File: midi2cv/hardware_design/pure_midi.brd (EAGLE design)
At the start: 78.9 x 100 mm, 117 parts, among them IC1 STM32F373C, IC2 AD5754BREZ, IC3 TL074D, IC4 TL072D, IC5 6N138SMD, IC6 LD117AS33TR, IC7 LD117AS50TR, IC8 ADR435, IC9 ADR431, J1 CORTEX_DEBUG_PTH, SW1 EC12E_SW, U2 AD5676ARUZ, U4 MAX3421, X1 ABRACON_ABM3B-8.000MHZ-B2-TAB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, X10 WQP-PJ301M-12_JACK, X11 WQP-PJ301M-12_JACK, X12 WQP-PJ301M-12_JACK, X13 WQP-PJ301M-12_JACK, X14 WQP-PJ301M-12_JACK, X15 WQP-PJ301M-12_JACK, X16 WQP-PJ301M-12_JACK, X17 WQP-PJ301M-12_JACK, X18 WQP-PJ301M-12_JACK, X19 WQP-PJ301M-12_JACK, X2 KUSBVX-BS1N, X20 WQP-PJ301M-12_JACK, X21 OG-MIDI_MAB5SHCUI-SD-50BV, X22 OG-MIDI_MAB5SHCUI-SD-50BV, X23 KUSBVX, X24 ABRACON_ABM3B-12.000MHZ-B2-TA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, X3 WQP-PJ301M-12_JACK, X4 WQP-PJ301M-12_JACK, X5 WQP-PJ301M-12_JACK, X6 WQP-PJ301M-12_JACK, X7 WQP-PJ301M-12_JACK, X8 WQP-PJ301M-12_JACK, X9 WQP-PJ301M-12_JACK

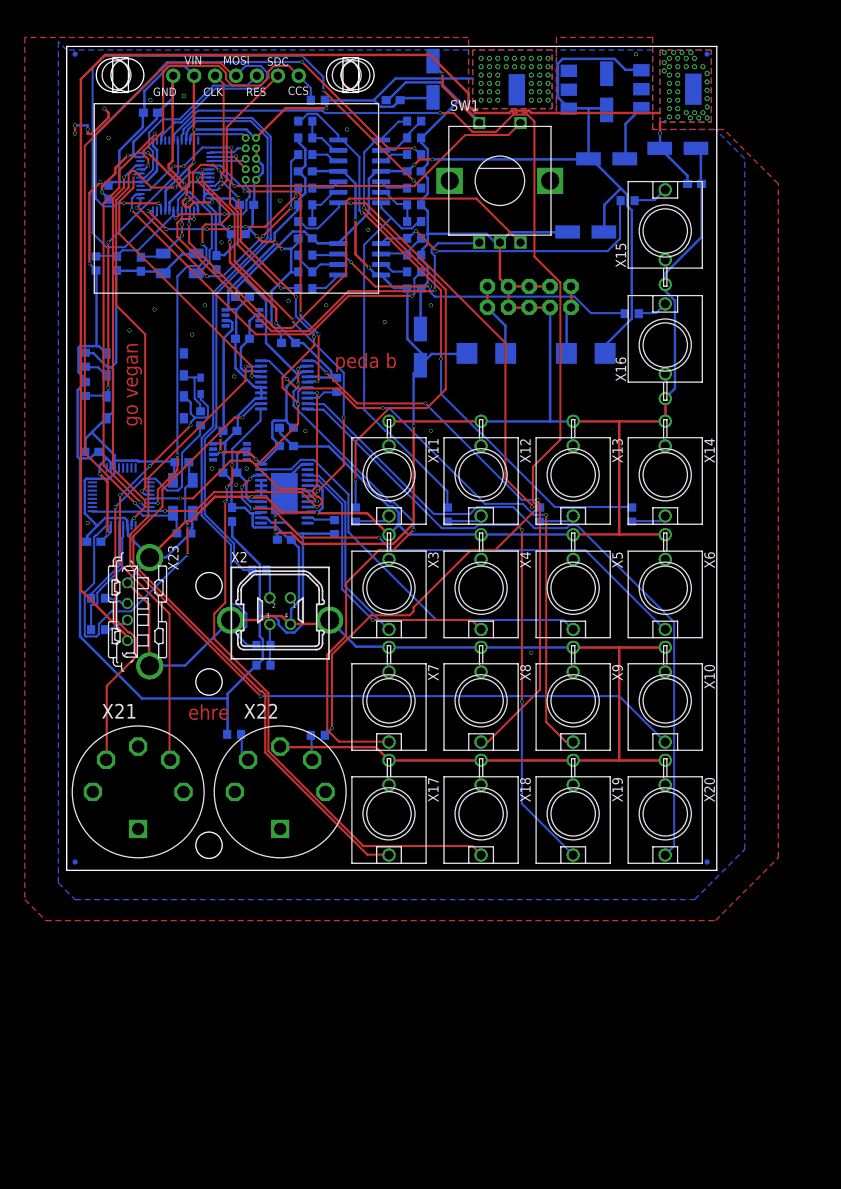
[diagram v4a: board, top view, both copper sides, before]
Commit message: Remove usb from midi
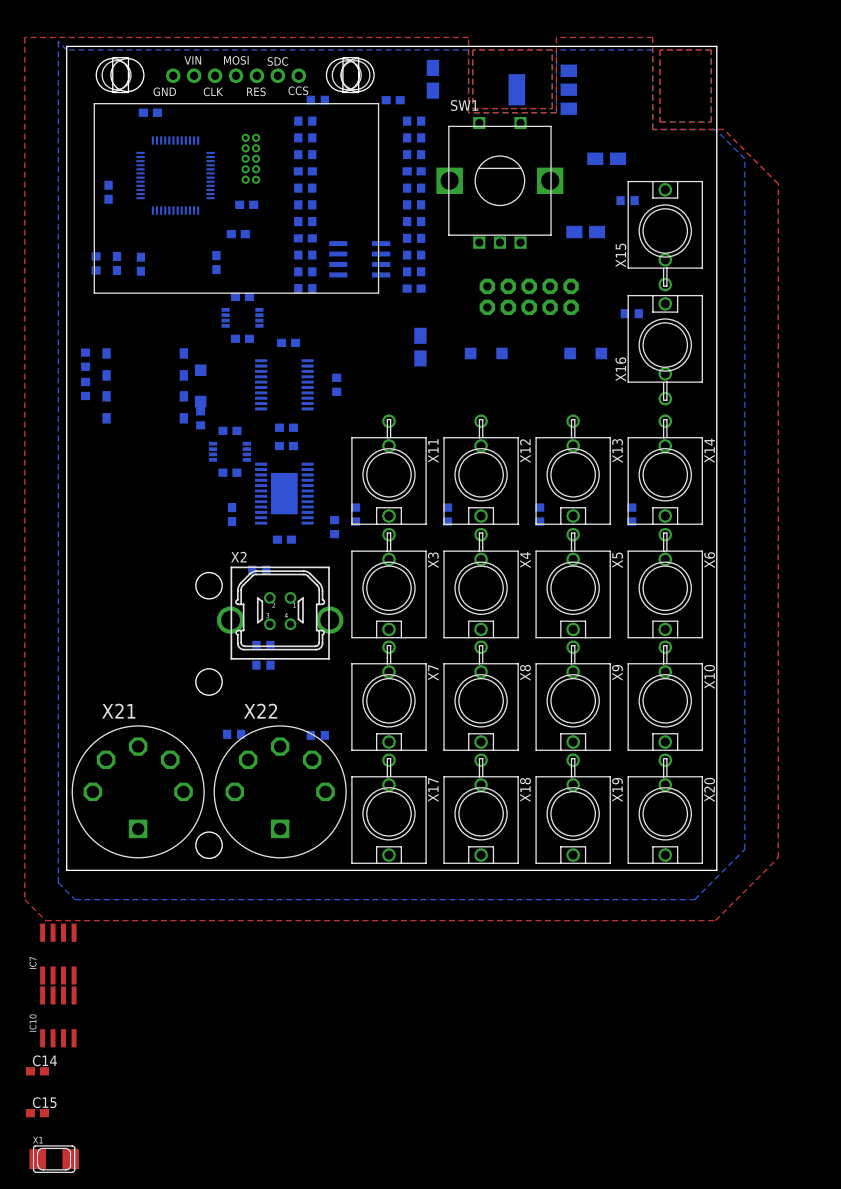
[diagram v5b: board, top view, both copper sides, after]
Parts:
- removed C16, C17: 100n, rcl:C0603
- removed C21, C23: 22u, GMSN:153CLV-0505
- removed C24: 100nF, rcl:C0603
- removed FD1, FD2, FD3, FD4: FIDUCIALUFIDUCIAL, SparkFun-Aesthetics:FIDUCIAL-MICRO
- removed IC3: TL074D, linear:SO14
- removed R21, R22: 22R, rcl:R0603
- removed U4: MAX3421, SparkFun-IC-Comms:TQFP32-5MM
- removed X23: KUSBVX, con-kycon:KUSBVX
- removed X24: ABRACON_ABM3B-12.000MHZ-B2-TABRACON_ABM3B-12.000MHZ-B2-T_0_0, Abracon - ABM3B-12.000MHZ-B2-T:ABRACON_ABM3B-12.000MHZ-B2-T_0
- added IC10: TL072CD, jhbruhn-opamp:SOIC8
- C1, C10, C11, C12, C13, C2, C25, C26, C27, C28, C29, C3, C30, C31, C32, C4, C5, C6, C7, C8, C9: device rcl:C0603 -> jhbruhn-cdr:C0603
- C14, C15: value 22p -> 100n; device rcl:C0603 -> jhbruhn-cdr:C0603
- C18, C19, C20, C22: value 22u -> 10uF; device GMSN:153CLV-0505 -> jhbruhn-cdr:CASE-A_3216
- D2: value 1N4148 -> 1N4148W; device adafruit:SOD-323F -> jhbruhn-cdr:SOD123
- D3, D4: value 1N4001 -> B5819W; device GMSN:SMADIODE -> jhbruhn-cdr:SOD123
- IC4: value TL072D -> TL072CD; device linear:SO08 -> jhbruhn-opamp:SOIC8
- IC7: value LD117AS50TR -> TL072CD; device v-reg:SOT223 -> jhbruhn-opamp:SOIC8
- R1, R10, R11, R12, R13, R14, R15, R16, R17, R18, R19, R2, R20, R23, R24, R25, R26, R27, R28, R29, R3, R30, R31, R32, R33, R34, R35, R36, R37, R38, R39, R4, R40, R6, R7: device rcl:R0603 -> jhbruhn-cdr:R0603
- R5: device resistor:R0603 -> jhbruhn-cdr:R0603
- X1: value ABRACON_ABM3B-8.000MHZ-B2-TABRACON_ABM3B-8.000MHZ-B2-T_0_0 -> 8MHz; device Abracon - ABM3B-8.000MHZ-B2-T:ABRACON_ABM3B-8.000MHZ-B2-T_0 -> jhbruhn-cdr:NX5032
- moved IC7 128.4 mm to (-1.02, -10.2), flipped to the top, turned to 0 degrees
- moved X1 109.8 mm to (-1.52, -35.1), flipped to the top, turned to 0 degrees
- moved C15 80.9 mm to (-3.56, -29.5), flipped to the top, turned to 0 degrees
- moved C14 67.7 mm to (-3.56, -24.4), flipped to the top
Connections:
- removed net +5V: C21.+, C24.1, IC7.4, X23.1
- removed net N$7: C14.2, U4.25, X24.1
- removed net USB_D_N: R22.1, X23.2
- removed net USB_D_P: R21.1, X23.3
- removed net USB_N: R22.2, U4.20
- removed net USB_P: R21.2, U4.21
- net +12V: now also C14.1, IC10.8, IC7.8; no longer C23.+, IC3.4, IC7.3
- net +3V3: no longer C16.1, C17.1, U4.2, U4.23
- net -12V: now also C15.2, IC10.4, IC7.4; no longer IC3.11
- net GND: now also C14.2; no longer C14.1, C16.2, C17.2, C18.-, C19.+, C21.-, C23.-, C24.2, IC7.1, PWR1.3, PWR1.4, PWR1.5, PWR1.6, PWR1.7, PWR1.8, U4.19, U4.3, X1.2, X1.4, X23.4, X23.M1, X23.M2, X24.2, X24.4
- net INT_USB: no longer U4.18
- net MISO: no longer U4.15
- net MOSI: no longer U4.16
- net N$10: now also IC10.1; no longer IC3.1
- net N$11: now also IC10.7; no longer IC3.7
- net N$14: now also IC10.6; no longer IC3.6
- net N$15: now also IC10.5; no longer IC3.5
- net N$16: now also IC10.2; no longer IC3.2
- net N$17: now also IC7.1; no longer IC3.8
- net N$18: now also IC7.2; no longer IC3.9
- net N$24: now also IC7.3; no longer IC3.10
- net N$25: now also IC10.3; no longer IC3.3
- net N$26: now also IC7.7; no longer IC3.14
- net N$27: now also IC7.6; no longer IC3.13
- net N$28: now also IC7.5; no longer IC3.12
- net N$3: now also X1.P$1; no longer X1.3
- net N$6: now also X1.P$2; no longer X1.1
- net N$8: now also C18.-, C19.+, PWR1.3, PWR1.4, PWR1.5, PWR1.6, PWR1.7, PWR1.8; no longer C15.2, U4.24, X24.3
- net RST_USB: no longer U4.12
- net SCK: no longer U4.13
- net SS_USB: no longer U4.14
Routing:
- net GND: track 706.1 -> 0.00 mm, vias 37 -> 0
- net +3V3: track 307.4 -> 0.00 mm, vias 54 -> 0
- net +12V: track 170.3 -> 0.00 mm, vias 5 -> 0
- net +5V: track 155.1 -> 0.00 mm, vias 39 -> 0
- net MIDI_DATA_OUT: track 140.5 -> 0.00 mm, vias 2 -> 0
- net MOSI: track 132.1 -> 0.00 mm, vias 4 -> 0
- net CV_OUT_8: track 105.7 -> 0.00 mm, vias 2 -> 0
- net -12V: track 88.5 -> 0.00 mm, vias 5 -> 0
- net SCK: track 86.9 -> 0.00 mm, vias 7 -> 0
- net CV_OUT_12: track 85.2 -> 0.00 mm
- net USB_PER_D_P: track 82.0 -> 0.00 mm
- net D_GATE_OUT_2: track 78.8 -> 0.00 mm, vias 2 -> 0
- net CV_OUT_10: track 77.7 -> 0.00 mm, vias 3 -> 0
- net CV_OUT_9: track 76.6 -> 0.00 mm, vias 1 -> 0
- net CV_OUT_11: track 74.5 -> 0.00 mm, vias 2 -> 0
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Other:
- board text removed: "ehre"
- board text removed: "go vegan"
- board text removed: "peda b"
